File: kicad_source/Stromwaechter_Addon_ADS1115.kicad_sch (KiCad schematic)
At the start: 19 parts, among them J1 Conn_01x04_MountingPin, J2 Conn_01x04_MountingPin, J3 Conn_01x04, J4 Conn_01x04, J5 Conn_01x04, J6 Conn_01x04, U1 ADS1115IDGS, U2 SRV05-4

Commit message: generated layout, added mounting holes
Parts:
- added H1, H2, H3, H4: MountingHole_Pad, MountingHole:MountingHole_3.2mm_M3_DIN965_Pad, symbol Mechanical:MountingHole_Pad
- J1, J2: value Conn_01x04_MountingPin -> SM04B-SRSS-TB; footprint (none) -> Connector_JST:JST_SH_SM04B-SRSS-TB_1x04-1MP_P1.00mm_Horizontal
- J3, J4, J5, J6: value Conn_01x04 -> MC_1,5_4-G-3.81; footprint (none) -> Connector_Phoenix_MC:PhoenixContact_MC_1,5_4-G-3.81_1x04_P3.81mm_Horizontal
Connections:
- net ADS1115_AIN4 is gone; now on net ADS1115_AIN3: J6.3 (Pin_3)
- net ADS1115_RSVD4 renamed ADS1115_RSVD3
- no-connect marks 5 -> 9
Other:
- moved on the sheet: C1, C2, C3, C4, C5, J1, J2, J3, J4, J5, J6, R1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

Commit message: added some capacitors on vcc and a testpoint at ads1115_alert
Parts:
- added C10, C11: 220 uF, Capacitor_SMD:CP_Elec_6.3x9.9, symbol Device:C_Polarized_Small
- added C6, C7, C8, C9: 100 nF, Capacitor_SMD:C_0603_1608Metric, symbol Device:C_Small
- added TP1: TestPoint, TestPoint:TestPoint_Pad_D1.5mm, symbol Connector:TestPoint
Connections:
- net +3.3V: now also C10.1, C11.1, C6.1, C7.1, C8.1, C9.1
- net GND: now also C10.2, C11.2, C6.2, C7.2, C8.2, C9.2
- net ADS1115_ALERT: now reaches U1.2 (ALERT/RDY)
- net ADS1115_ALERT: now also TP1.1
- no-connect marks 9 -> 8

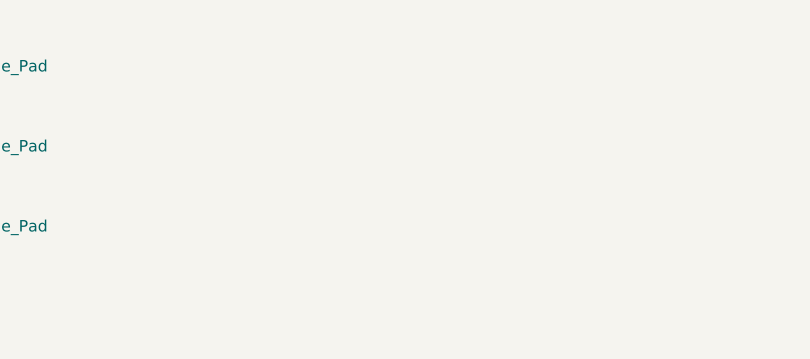
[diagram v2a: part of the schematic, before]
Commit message: added labels, made DRC
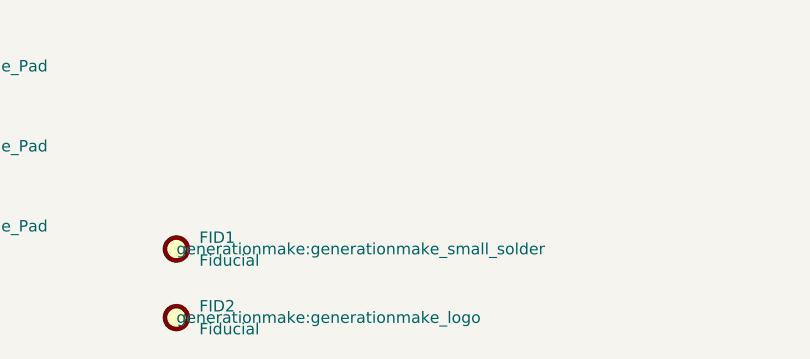
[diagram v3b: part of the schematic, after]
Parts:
- added FID1: Fiducial, generationmake:generationmake_small_solder, symbol Mechanical:Fiducial
- added FID2: Fiducial, generationmake:generationmake_logo, symbol Mechanical:Fiducial
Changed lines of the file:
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@@
 	)
 	(symbol
+		(lib_id "Mechanical:Fiducial")
+		(at 54.61 191.77 0)
+		(unit 1)
+		(exclude_from_sim yes)
+		(in_bom no)
+		(on_board yes)
+		(dnp no)
+		(fields_autoplaced yes)
+		(property "Reference" "FID2"
+			(at 57.15 190.4999 0)
+			(effects
+				(font
+					(size 1.27 1.27)
+				)
+				(justify left)
+			)
+		)
+		(property "Value" "Fiducial"
+			(at 57.15 193.0399 0)
+			(effects
+				(font
+					(size 1.27 1.27)
+				)
+				(justify left)
+			)
+		)
+		(property "Footprint" "generationmake:generationmake_logo"
+			(at 54.61 191.77 0)
+			(effects
+				(font
+					(size 1.27 1.27)
+				)
+				(justify left)
+			)
+		)
+		(property "Datasheet" "~"
+			(at 54.61 191.77 0)
+			(effects
+				(font
+					(size 1.27 1.27)
+				)
+				(hide yes)
+			)
+		)
+		(property "Description" "Fiducial Marker"
+			(at 54.61 191.77 0)
+			(effects
+				(font
+					(size 1.27 1.27)
+				)
+				(hide yes)
+			)
+		)
+		(instances
+			(project "Stromwaechter_Addon_ADS1115"
+				(path "/f637cfca-2e8e-4408-9cbe-c1f07a75d1ae"
+					(reference "FID2")
+					(unit 1)
+				)
+			)
+		)
+	)
+	(symbol
 		(lib_id "Mechanical:MountingHole_Pad")
 		(at 21.59 181.61 0)
@@
 					(unit 1)
 				)
+			)
+		)
+	)
+	(symbol
+		(lib_id "Mechanical:Fiducial")
+		(at 54.61 184.15 0)
+		(unit 1)
+		(exclude_from_sim yes)
+		(in_bom no)
+		(on_board yes)
+		(dnp no)
+		(fields_autoplaced yes)
+		(property "Reference" "FID1"
+			(at 57.15 182.8799 0)
+			(effects
+				(font
+					(size 1.27 1.27)
+				)
+				(justify left)
+			)
+		)
+		(property "Value" "Fiducial"
+			(at 57.15 185.4199 0)
+			(effects
+				(font
+					(size 1.27 1.27)
+				)
+				(justify left)
+			)
+		)
+		(property "Footprint" "generationmake:generationmake_small_solder"
+			(at 54.61 184.15 0)
+			(effects
+				(font
+					(size 1.27 1.27)
+				)
+				(justify left)
+			)
+		)
+		(property "Datasheet" "~"
+			(at 54.61 184.15 0)
+			(effects
+				(font
+					(size 1.27 1.27)
+				)
+				(hide yes)
+			)
+		)
+		(property "Description" "Fiducial Marker"
+			(at 54.61 184.15 0)
+			(effects
+				(font
+					(size 1.27 1.27)
+				)
+				(hide yes)
+			)
+		)
+		(instances
+			(project ""
+				(path "/f637cfca-2e8e-4408-9cbe-c1f07a75d1ae"
+					(reference "FID1")
+					(unit 1)
+				)
